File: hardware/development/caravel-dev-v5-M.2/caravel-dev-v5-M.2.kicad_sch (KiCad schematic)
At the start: 64 parts, among them J1 USB_B_Micro - 10118193-0001LF, J10 Conn_01x27_Female, J11 Conn_01x20_Female, J2 Conn_01x02_Female, J3 Conn_01x02_Male, J4 Conn_01x03_Female, J5 Conn_01x02_Male, J6 Conn_01x02_Male, J7 Conn_01x06_Female, J8 Conn_01x02_Male, J9 Conn_01x02_Male, SW1 SW_Push - SKQGADE010, T1 Logo, T2 Logo, U1 FT232H, U2 SN74LVC1G125DCKR, U3 SN74LVC1G125DCKR, U4 MCP1319MT-29LE-OT, U5 TAR5SxxU_SOT353F, U6 TAR5SxxU_SOT353F, U7 W25Q32FVSS, U8 caravel-M.2-card, X1 DSC6001_10MHZ, Y1 CSTNE12M0GH5L000R0

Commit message: ~ update caravel v5 board: ~ fix UART mode issue by enabling it by default (pull `~UART_EN` down) and in SPI mode,   the FTDI drives `~UART_EN` high. This is required since the FTDI GPIOs are not   configurable in UART mode. - remove on-board PoR U4 and use the on-chip PoR
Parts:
- removed J10: Conn_01x27_Female, Connector_PinHeader_2.54mm:PinHeader_1x27_P2.54mm_Vertical, symbol Connector:Conn_01x28_Female
- removed J11: Conn_01x20_Female, Connector_PinHeader_2.54mm:PinHeader_1x20_P2.54mm_Vertical, symbol Connector:Conn_01x28_Female
- removed J2: Conn_01x02_Female, Connector_PinHeader_2.54mm:PinHeader_1x02_P2.54mm_Vertical, symbol Connector:Conn_01x02_Female
- removed J3, J5, J6: Conn_01x02_Male, Connector_PinHeader_2.54mm:PinHeader_1x02_P2.54mm_Vertical, symbol Connector:Conn_01x02_Male
- removed J7: Conn_01x06_Female, Connector_PinHeader_2.54mm:PinHeader_1x06_P2.54mm_Vertical, symbol Connector:Conn_01x06_Female
- removed U4: MCP1319MT-29LE-OT, Caravel_Board:PoR_5_SOT23, symbol Caravel_board:MCP1319MT-29LE-OT
- removed U8: caravel-M.2-card, MicroMod-Sparkfun:M.2-CONNECTOR-E, symbol Caravel_board:caravel-M.2-card
- added C18, C21: 0.1uF, Capacitor_SMD:C_0805_2012Metric, symbol Device:C
- added C19: 1uF, Capacitor_SMD:C_0805_2012Metric, symbol Device:C
- added C20: 0.01uF, Capacitor_SMD:C_0805_2012Metric, symbol Device:C
- added C22: 10uF, Capacitor_SMD:C_0805_2012Metric, symbol Device:C
- added FB1: 600R/0.5A, Inductor_SMD:L_0805_2012Metric, symbol Device:FerriteBead
- added J10, J11: Conn_01x28_Pin, Connector_PinHeader_2.54mm:PinHeader_1x28_P2.54mm_Vertical, symbol Connector:Conn_01x28_Socket
- added J2, J3, J5, J6: Conn_01x02_Pin, Connector_PinHeader_2.54mm:PinHeader_1x02_P2.54mm_Vertical, symbol Connector:Conn_01x02_Pin
- added J7: Conn_01x06_Pin, Connector_PinHeader_2.54mm:PinHeader_1x06_P2.54mm_Vertical, symbol Connector:Conn_01x06_Pin
- added U8: M.2-CONNECTOR-E, MicroMod-Sparkfun:M.2-CONNECTOR-E, symbol MicroMod-Sparkfun:M.2-CONNECTOR-E
- C1: value 0.01uf - CC0805JRX7R9BB103 -> 0.01uF; Part # (none) -> C0805C103K5RAC7411
- C10, C13: value 1uf - CC0805KKX5R8BB105 -> 1uF; Part # (none) -> 885012207103
- C11, C14: value 0.01uf - CC0805KRX7R9BB103 -> 0.01uF; Part # (none) -> C0805C103K5RAC7411
- C12, C15: value 10uf - CC0805KKX5R8BB106 -> 10uF; Part # (none) -> CL21B106KAYQNNE
- C16: value 0.1uf - CC0805KRX7R9BB104 -> 10uF; Part # (none) -> CL21B106KAYQNNE
- C17: value 0.1uf - CC0805KRX7R9BB104 -> 0.01uF; Part # (none) -> C0805C103K5RAC7411
- C2, C3, C4, C5, C6, C7, C8, C9: value 0.1uf - CC0805KRX7R9BB104 -> 0.1uF; Part # (none) -> C0805C104K5RAC7411
- D1, D2, D3, D4: value LED - 17-215SURC/S530-A2/TR8 -> RED; Part # (none) -> LTST-C230KRKT
- J1: value USB_B_Micro - 10118193-0001LF -> USB_B_Micro; Part # (none) -> 10118193-0001LF
- J4: value Conn_01x03_Female -> Conn_01x03_Pin
- J8, J9: value Conn_01x02_Male -> Conn_01x02_Pin; symbol Connector:Conn_01x02_Male -> Connector:Conn_01x02_Pin
- R1, R10, R12, R13, R7, R8, R9: value 10k - RC0805FR-0710KL -> 10K; Part # (none) -> RC0805FR-0710KL
- R11, R14: value 82 - 0805W8F820JT5E -> 1K; Part # (none) -> RC0805FR-071KL
- R15, R16: value 10k -> 10K; Part # (none) -> RC0805FR-0710KL
- R2: value 12K 1% - 0805W8F1202T5E -> 12K 1%; Part # (none) -> RMCF0805FT12K0
- R3, R4: value 150 - 0805W8J0151T5E -> 150; Part # (none) -> RNCP0805FTD150R
- R5, R6: value 10k -> 1K; Part # (none) -> RC0805FR-071KL
- U1: Part # (none) -> FT232H
- U2, U3: Part # (none) -> SN74LVC1G125DCKR
- U5: value TAR5SxxU_SOT353F -> TAR5SxxU; Part # (none) -> TAR5S33UTE85LF
- U6: value TAR5SxxU_SOT353F -> TAR5SxxU; Part # (none) -> TAR5S18U-TE85L-F
- U7: Part # (none) -> W25Q32JVSSIQ
- X1: Part # (none) -> DSC6001JI1B
- Y1: value CSTNE12M0GH5L000R0 -> 12MHz; Part # (none) -> CSTNE12M0GH5L000R0
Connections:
- net +1V8: now also J11.22 (Pin_22), J11.23 (Pin_23), J11.24 (Pin_24), J3.1 (Pin_1), J3.2 (Pin_2), U8.14 (P14), U8.15 (P15), U8.35 (P27)
- net +5V: now also C21.2, C22.2, FB1.2; no longer J1.1 (VBUS)
- net Caravel_CSB: now also J7.1 (Pin_1), U8.11 (P11)
- net Caravel_D0: now also J7.6 (Pin_6), U8.17 (P17)
- net Caravel_D1: now also J7.2 (Pin_2), U8.19 (P19)
- net Caravel_SCK: now also J7.5 (Pin_5), U8.23 (P23)
- net GND: now also C16.2, C17.1, R5.1, R6.1, C18.2, C19.2, C20.2, C21.1, C22.1, J10.28 (Pin_28), J10.6 (Pin_6), J11.1 (Pin_1), J11.17 (Pin_17), J11.18 (Pin_18), J11.28 (Pin_28), J6.2 (Pin_2), U8.12 (P12), U8.18 (P18), U8.37 (P29), U8.A1 (GND), U8.A2 (GND); no longer C16.1, C17.2
- net USB_CS1: now also J11.12 (Pin_12), U8.55 (P47)
- net USB_SCK_TXD: now also J11.11 (Pin_11), U8.57 (P49)
- net USB_SI: now also J11.14 (Pin_14), U8.51 (P43)
- net USB_SO_RXD: now also J11.13 (Pin_13), U8.53 (P45)
- net gpio: now also J11.20 (Pin_20), U8.21 (P21)
- net mprj_io[0]: now also J11.15 (Pin_15), U8.49 (P41)
- net mprj_io[10]: now also J11.5 (Pin_5), U8.69 (P61)
- net mprj_io[11]: now also J11.4 (Pin_4), U8.71 (P63)
- net mprj_io[12]: now also J11.3 (Pin_3), U8.73 (P65)
- net mprj_io[13]: now also J11.2 (Pin_2), U8.75 (P67)
- net mprj_io[14]: now also J10.27 (Pin_27), U8.74 (P66)
- net mprj_io[15]: now also J10.26 (Pin_26), U8.72 (P64)
- net mprj_io[16]: now also J10.25 (Pin_25), U8.70 (P62)
- net mprj_io[17]: now also J10.24 (Pin_24), U8.68 (P60)
- net mprj_io[18]: now also J10.23 (Pin_23), U8.66 (P58)
- net mprj_io[19]: now also J10.22 (Pin_22), U8.64 (P56)
- net mprj_io[20]: now also J10.21 (Pin_21), U8.62 (P54)
- net mprj_io[21]: now also J10.20 (Pin_20), U8.60 (P52)
- net mprj_io[22]: now also J10.19 (Pin_19), U8.58 (P50)
- net mprj_io[23]: now also J10.18 (Pin_18), U8.56 (P48)
- net mprj_io[24]: now also J10.17 (Pin_17), U8.54 (P46)
- net mprj_io[25]: now also J10.16 (Pin_16), U8.52 (P44)
- net mprj_io[26]: now also J10.15 (Pin_15), U8.50 (P42)
- net mprj_io[27]: now also J10.14 (Pin_14), U8.48 (P40)
- net mprj_io[28]: now also J10.13 (Pin_13), U8.46 (P38)
- net mprj_io[29]: now also J10.12 (Pin_12), U8.44 (P36)
- net mprj_io[30]: now also J10.11 (Pin_11), U8.42 (P34)
- net mprj_io[31]: now also J10.10 (Pin_10), U8.40 (P32)
- net mprj_io[32]: now also J10.9 (Pin_9), U8.38 (P30)
- net mprj_io[33]: now also J10.8 (Pin_8), U8.36 (P28)
- net mprj_io[34]: now also J10.4 (Pin_4), U8.34 (P26)
- net mprj_io[35]: now also J10.3 (Pin_3), U8.32 (P24)
- net mprj_io[36]: now also J10.2 (Pin_2), U8.22 (P22)
- net mprj_io[37]: now also J10.1 (Pin_1), U8.20 (P20)
- net mprj_io[5]_ser_rx: now also J11.10 (Pin_10), U8.59 (P51)
- net mprj_io[6]_ser_tx: now also J11.9 (Pin_9), U8.61 (P53)
- net mprj_io[7]: now also J11.8 (Pin_8), U8.63 (P55)
- net mprj_io[8]: now also J11.7 (Pin_7), U8.65 (P57)
- net mprj_io[9]: now also J11.6 (Pin_6), U8.67 (P59)
- net vccd2: now also J11.21 (Pin_21), U8.1 (P1)
- net vdda1: now also J11.16 (Pin_16), U8.33 (P25)
- net vdda2: now also J11.25 (Pin_25), U8.13 (P13)
- net xclk: now also J11.19 (Pin_19), U8.9 (P9)
- net ~{MEM_HOLD}: now also J7.4 (Pin_4)
- net ~{MEM_WP}: now also J7.3 (Pin_3)
- net VCCA: now reaches C3.2, U1.37 (VCCA)
- net OSC_EN: now reaches X1.1 (EN)
- net OSC_EN: now also J6.1 (Pin_1)
- net Noise_3V3: now reaches C11.1, U5.3 (Noise)
- net ~{FTDI_RST}: now reaches C1.2, R1.1, U1.34 (~{RESET})
- net VCCCORE: now reaches C2.2, U1.38 (VCCCORE)
- net ACBUS2: now reaches D1.1 (K)
- net ACBUS2: now also U1.26 (ACBUS2); no longer U1.27 (ACBUS3)
- net Noise_1V8: now reaches C14.1, U6.3 (Noise)
- net ADBUS4: now reaches U1.17 (ADBUS4)
- net ADBUS5: now reaches U1.18 (ADBUS5)
- net ADBUS6: now reaches U1.19 (ADBUS6)
- net ADBUS7: now reaches U1.20 (ADBUS7)
- net ACBUS3: now reaches D2.1 (K)
- net ACBUS3: now also U1.27 (ACBUS3); no longer U1.26 (ACBUS2)
- net ACBUS4: now reaches U1.28 (ACBUS4)
- net ACBUS5: now reaches U1.29 (ACBUS5)
- net ACBUS6: now reaches U1.30 (ACBUS6)
- net ACBUS7: now reaches U1.31 (ACBUS7)
- net +3.3V renamed +3V3
- net +3V3: now also C16.1, C17.2, C18.1, C19.1, J10.7 (Pin_7), J11.26 (Pin_26), J11.27 (Pin_27), J2.1 (Pin_1), J5.1 (Pin_1), J5.2 (Pin_2), U8.16 (P16), U8.3 (P3), U8.5 (P5); no longer C16.2, C17.1, R5.1, R6.1
- net UART_EN renamed ACBUS0
- net ACBUS0: now also J2.2 (Pin_2)
- net ~{MR} renamed ACBUS1
- net ACBUS1: now also J10.5 (Pin_5), U8.7 (P7)
- new net VBUS: C20.1, FB1.1, J1.1 (VBUS)
- no-connect marks 26 -> 17
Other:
- note added: "*ACBUS7 pulled-down"
- note added: "*ACBUS8-9 are not configurable as GPIOs in MPSSE mode"
- note added: "*Place close to the USB connector"
- note added: "*enabled by default and should be disabled in SPI mode"
- note added: "*required since the FTDI UART ports are shared with the SPI"
- note added: "Buffers to enable FTDI UART interface with Caravel"
- note added: "Caravel M.2 Card"
- note added: "Caravel Power Pin Headers"
- note added: "FTDI SPI interface with HKSPI"
- note added: "GPIO Connectors"
- note added: "Interfaces"
- note added: "M.2 Connector + Peripherals"
- note added: "Pin Headers"
- note added: "Power"
- note added: "Reset"
- note added: "Reset Switch"
- note added: "USB to Serial"
- note added: "VBUS Filter to 5V"
- note added: "Voltage Regulators"
- note added: "internally with 75k by default"
- note removed: "Buffers to enable FTDI UART interface"
- note removed: "FTDI interface with HKSPI"
- note removed: "IO Connectors"
- note removed: "Power Pin Headers"
- note removed: "Power on Reset"
- note removed: "Voltage Regulator"
- company: (none) -> Efabless
- title: (none) -> Caravel 3.3V Development Board
- moved on the sheet: C10, C11, C12, C13, C14, C15, J8, J9, R15, R16, U5, U6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

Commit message: ~ update caravel REV5B board files
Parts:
- added TP3, TP4, TP5, TP6: TestPoint, TestPoint:TestPoint_Loop_D1.80mm_Drill1.0mm_Beaded, symbol Connector:TestPoint
- U2, U3: footprint SOT65P210X110-5N -> strive_foot_prints:SOT65P210X110-5N
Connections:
- net +3V3: now also J10.3 (Pin_3); no longer J10.7 (Pin_7)
- net ACBUS1: now also J10.1 (Pin_1); no longer J10.5 (Pin_5)
- net ADBUS4: now also TP3.1
- net ADBUS5: now also TP4.1
- net ADBUS6: now also TP5.1
- net ADBUS7: now also TP6.1
- net GND: now also J10.2 (Pin_2); no longer J10.6 (Pin_6)
- net mprj_io[34]: now also J10.7 (Pin_7); no longer J10.4 (Pin_4)
- net mprj_io[35]: now also J10.6 (Pin_6); no longer J10.3 (Pin_3)
- net mprj_io[36]: now also J10.5 (Pin_5); no longer J10.2 (Pin_2)
- net mprj_io[37]: now also J10.4 (Pin_4); no longer J10.1 (Pin_1)

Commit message: ~ update caravel REV5B
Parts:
- removed TP3, TP4, TP5, TP6: TestPoint, TestPoint:TestPoint_Loop_D1.80mm_Drill1.0mm_Beaded, symbol Connector:TestPoint
- added J12: Conn_01x04_Pin, Connector_PinHeader_2.54mm:PinHeader_1x04_P2.54mm_Vertical, symbol Connector:Conn_01x04_Pin
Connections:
- net ADBUS4: now also J12.1 (Pin_1)
- net ADBUS5: now also J12.2 (Pin_2)
- net ADBUS6: now also J12.3 (Pin_3)
- net ADBUS7: now also J12.4 (Pin_4)
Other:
- note added: "*exposed GPIOs"
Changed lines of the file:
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@@
   (junction (at 260.731 196.596) (diameter 0) (color 0 0 0 0)
   )
+  (junction (at 223.774 244.856) (diameter 0) (color 0 0 0 0)
+  )
   (junction (at 279.781 106.426) (diameter 0) (color 0 0 0 0)
   )
@@
   (junction (at 356.616 208.28) (diameter 0) (color 0 0 0 0)
   )
-  (junction (at 151.13 75.438) (diameter 0) (color 0 0 0 0)
-  )
   (junction (at 272.161 92.456) (diameter 0) (color 0 0 0 0)
   )
+  (junction (at 226.314 244.856) (diameter 0) (color 0 0 0 0)
+  )
   (junction (at 303.784 149.606) (diameter 0) (color 0 0 0 0)
   )
@@
   (junction (at 253.111 196.596) (diameter 0) (color 0 0 0 0)
   )
-  (junction (at 285.115 244.348) (diameter 0) (color 0 0 0 0)
-  )
-  (junction (at 129.54 77.978) (diameter 0) (color 0 0 0 0)
-  )
   (junction (at 162.052 247.142) (diameter 0) (color 0 0 0 0)
   )
@@
   (junction (at 373.634 190.5) (diameter 0) (color 0 0 0 0)
   )
-  (junction (at 287.655 244.348) (diameter 0) (color 0 0 0 0)
-  )
   (junction (at 382.016 164.465) (diameter 0) (color 0 0 0 0)
   )
@@
   (junction (at 330.708 164.338) (diameter 0) (color 0 0 0 0)
   )
-  (junction (at 151.13 77.978) (diameter 0) (color 0 0 0 0)
+  (junction (at 129.54 77.978) (diameter 0) (color 0 0 0 0)
   )
-  (junction (at 223.774 244.856) (diameter 0) (color 0 0 0 0)
+  (junction (at 285.115 244.348) (diameter 0) (color 0 0 0 0)
   )
-  (junction (at 226.314 244.856) (diameter 0) (color 0 0 0 0)
+  (junction (at 151.13 77.978) (diameter 0) (color 0 0 0 0)
+  )
+  (junction (at 287.655 244.348) (diameter 0) (color 0 0 0 0)
   )
   (junction (at 263.271 196.596) (diameter 0) (color 0 0 0 0)
@@
   (junction (at 248.031 110.236) (diameter 0) (color 0 0 0 0)
   )
+  (junction (at 151.13 75.438) (diameter 0) (color 0 0 0 0)
+  )
   (junction (at 239.395 246.888) (diameter 0) (color 0 0 0 0)
   )
@@
     (stroke (width 0) (type default))
   )
+  (wire (pts (xy 285.115 244.348) (xy 287.655 244.348))
+    (stroke (width 0) (type default))
+  )
   (wire (pts (xy 71.12 36.068) (xy 54.61 36.068))
     (stroke (width 0) (type default))
@@
     (stroke (width 0) (type default))
   )
+  (wire (pts (xy 129.54 75.438) (xy 129.54 77.978))
+    (stroke (width 0) (type default))
+  )
   (wire (pts (xy 282.575 244.348) (xy 285.115 244.348))
     (stroke (width 0) (type default))
@@
     (stroke (width 0) (type default))
   )
+  (wire (pts (xy 223.774 244.856) (xy 226.314 244.856))
+    (stroke (width 0) (type default))
+  )
   (wire (pts (xy 92.456 161.29) (xy 83.82 161.29))
     (stroke (width 0) (type default))
@@
     (stroke (width 0) (type default))
   )
+  (wire (pts (xy 151.13 75.438) (xy 151.13 77.978))
+    (stroke (width 0) (type default))
+  )
   (wire (pts (xy 273.431 129.286) (xy 282.829 129.286))
     (stroke (width 0) (type default))
@@
     (stroke (width 0) (type default))
   )
-  (wire (pts (xy 129.54 75.438) (xy 129.54 77.978))
-    (stroke (width 0) (type default))
-  )
   (wire (pts (xy 58.293 132.715) (xy 58.293 134.239))
     (stroke (width 0) (type default))
@@
     (stroke (width 0) (type default))
   )
-  (wire (pts (xy 151.13 75.438) (xy 151.13 77.978))
-    (stroke (width 0) (type default))
-  )
   (polyline (pts (xy 187.833 112.903) (xy 15.113 112.903))
     (stroke (width 0) (type dash))
@@
     (stroke (width 0) (type default))
   )
-  (wire (pts (xy 285.115 244.348) (xy 287.655 244.348))
-    (stroke (width 0) (type default))
-  )
   (wire (pts (xy 135.89 77.978) (xy 129.54 77.978))
     (stroke (width 0) (type default))
@@
     (stroke (width 0) (type default))
   )
-  (wire (pts (xy 223.774 244.856) (xy 226.314 244.856))
-    (stroke (width 0) (type default))
-  )
   (wire (pts (xy 178.054 257.556) (xy 200.914 257.556))
     (stroke (width 0) (type default))
@@
     (effects (font (size 1.5 1.5)) (justify left bottom))
   )
+  (text "*exposed GPIOs" (at 287.909 136.144 0)
+    (effects (font (size 1.25 1.25)) (justify left bottom))
+  )
   (text "Power" (at 116.459 225.171 0)
     (effects (font (size 3.5 3.5) (thickness 0.7) bold italic) (justify left bottom))
@@
     )
   )
-  (symbol (lib_id "Connector:TestPoint") (at 281.432 139.446 270) (unit 1)
-    (in_bom yes) (on_board yes) (dnp no)
-    (property "Reference" "TP6" (at 286.004 139.573 90)
-      (effects (font (size 1.27 1.27)) (justify left))
-    )
-    (property "Value" "TestPoint" (at 286.893 140.716 90)
-      (effects (font (size 1.27 1.27)) (justify left) hide)
-    )
-    (property "Footprint" "TestPoint:TestPoint_Loop_D1.80mm_Drill1.0mm_Beaded" (at 281.432 144.526 0)
-      (effects (font (size 1.27 1.27)) hide)
-    )
-    (property "Datasheet" "~" (at 281.432 144.526 0)
-      (effects (font (size 1.27 1.27)) hide)
-    )
-    (pin "1")
-    (instances
-      (project "caravel-dev-v5-M.2"
-        (path "/6d7a4d05-3bd6-4623-a293-816712af04ea"
-          (reference "TP6") (unit 1)
-        )
-      )
-    )
-  )
   (symbol (lib_id "Connector:USB_B_Micro") (at 212.979 100.584 0) (unit 1)
     (in_bom yes) (on_board yes) (dnp no)
@@
     )
   )
+  (symbol (lib_id "Connector:Conn_01x04_Pin") (at 286.512 134.366 0) (mirror y) (unit 1)
+    (in_bom yes) (on_board yes) (dnp no)
+    (property "Reference" "J12" (at 289.433 132.08 0)
+      (effects (font (size 1.27 1.27)))
+    )
+    (property "Value" "Conn_01x04_Pin" (at 291.973 135.636 90)
+      (effects (font (size 1.27 1.27)) hide)
+    )
+    (property "Footprint" "Connector_PinHeader_2.54mm:PinHeader_1x04_P2.54mm_Vertical" (at 286.512 134.366 0)
+      (effects (font (size 1.27 1.27)) hide)
+    )
+    (property "Datasheet" "~" (at 286.512 134.366 0)
+      (effects (font (size 1.27 1.27)) hide)
+    )
+    (pin "1")
+    (pin "3")
+    (pin "2")
+    (pin "4")
+    (instances
+      (project "caravel-dev-v5-M.2"
+        (path "/6d7a4d05-3bd6-4623-a293-816712af04ea"
+          (reference "J12") (unit 1)
+        )
+      )
+    )
+  )
   (symbol (lib_id "power:GND") (at 149.86 259.334 0) (unit 1)
     (in_bom yes) (on_board yes) (dnp no)
@@
     )
   )
-  (symbol (lib_id "Connector:TestPoint") (at 281.432 134.366 270) (unit 1)
-    (in_bom yes) (on_board yes) (dnp no)
-    (property "Reference" "TP4" (at 286.004 134.493 90)
-      (effects (font (size 1.27 1.27)) (justify left))
-    )
-    (property "Value" "TestPoint" (at 286.893 135.636 90)
-      (effects (font (size 1.27 1.27)) (justify left) hide)
-    )
-    (property "Footprint" "TestPoint:TestPoint_Loop_D1.80mm_Drill1.0mm_Beaded" (at 281.432 139.446 0)
-      (effects (font (size 1.27 1.27)) hide)
-    )
-    (property "Datasheet" "~" (at 281.432 139.446 0)
-      (effects (font (size 1.27 1.27)) hide)
-    )
-    (pin "1")
-    (instances
-      (project "caravel-dev-v5-M.2"
-        (path "/6d7a4d05-3bd6-4623-a293-816712af04ea"
-          (reference "TP4") (unit 1)
-        )
-      )
-    )
-  )
   (symbol (lib_id "Device:R") (at 299.212 157.607 90) (unit 1)
     (in_bom yes) (on_board yes) (dnp no)
@@
     )
   )
-  (symbol (lib_id "Connector:TestPoint") (at 281.432 131.826 270) (unit 1)
-    (in_bom yes) (on_board yes) (dnp no)
-    (property "Reference" "TP3" (at 286.004 131.826 90)
-      (effects (font (size 1.27 1.27)) (justify left))
-    )
-    (property "Value" "TestPoint" (at 286.893 133.096 90)
-      (effects (font (size 1.27 1.27)) (justify left) hide)
-    )
-    (property "Footprint" "TestPoint:TestPoint_Loop_D1.80mm_Drill1.0mm_Beaded" (at 281.432 136.906 0)
-      (effects (font (size 1.27 1.27)) hide)
-    )
-    (property "Datasheet" "~" (at 281.432 136.906 0)
-      (effects (font (size 1.27 1.27)) hide)
-    )
-    (pin "1")
-    (instances
-      (project "caravel-dev-v5-M.2"
-        (path "/6d7a4d05-3bd6-4623-a293-816712af04ea"
-          (reference "TP3") (unit 1)
-        )
-      )
-    )
-  )
   (symbol (lib_id "Device:C") (at 208.153 125.222 90) (unit 1)
     (in_bom yes) (on_board yes) (dnp no)
@@
         )
       )
-    )
-  )
-  (symbol (lib_id "Connector:TestPoint") (at 281.432 136.906 270) (unit 1)
-    (in_bom yes) (on_board yes) (dnp no)
-    (property "Reference" "TP5" (at 286.004 137.033 90)
-      (effects (font (size 1.27 1.27)) (justify left))
-    )
-    (property "Value" "TestPoint" (at 286.893 138.176 90)
-      (effects (font (size 1.27 1.27)) (justify left) hide)
-    )
-    (property "Footprint" "TestPoint:TestPoint_Loop_D1.80mm_Drill1.0mm_Beaded" (at 281.432 141.986 0)
-      (effects (font (size 1.27 1.27)) hide)
-    )
-    (property "Datasheet" "~" (at 281.432 141.986 0)
-      (effects (font (size 1.27 1.27)) hide)
-    )
-    (pin "1")
-    (instances
-      (project "caravel-dev-v5-M.2"
-        (path "/6d7a4d05-3bd6-4623-a293-816712af04ea"
-          (reference "TP5") (unit 1)
-        )
-      )

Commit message: ~ update caravel REV 5B with larger logos
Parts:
- T1: footprint Caravel_Board:logo -> Caravel_Board:logo_large
- T2: footprint Caravel_Board:ef_logo -> Caravel_Board:ef_logo_large
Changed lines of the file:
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@@
       (effects (font (size 1.27 1.27)) (justify left))
     )
-    (property "Footprint" "Caravel_Board:logo" (at 144.145 32.258 0)
+    (property "Footprint" "Caravel_Board:logo_large" (at 144.145 32.258 0)
       (effects (font (size 1.27 1.27)) hide)
     )
@@
       (effects (font (size 1.27 1.27)) (justify left))
     )
-    (property "Footprint" "Caravel_Board:ef_logo" (at 156.845 32.258 0)
-      (effects (font (size 1.27 1.27)) hide)
-    )
+    (property "Footprint" "Caravel_Board:ef_logo_large" (at 156.845 32.258 0)
+      (effects (font (size 1.27 1.27)) hide)
+    )

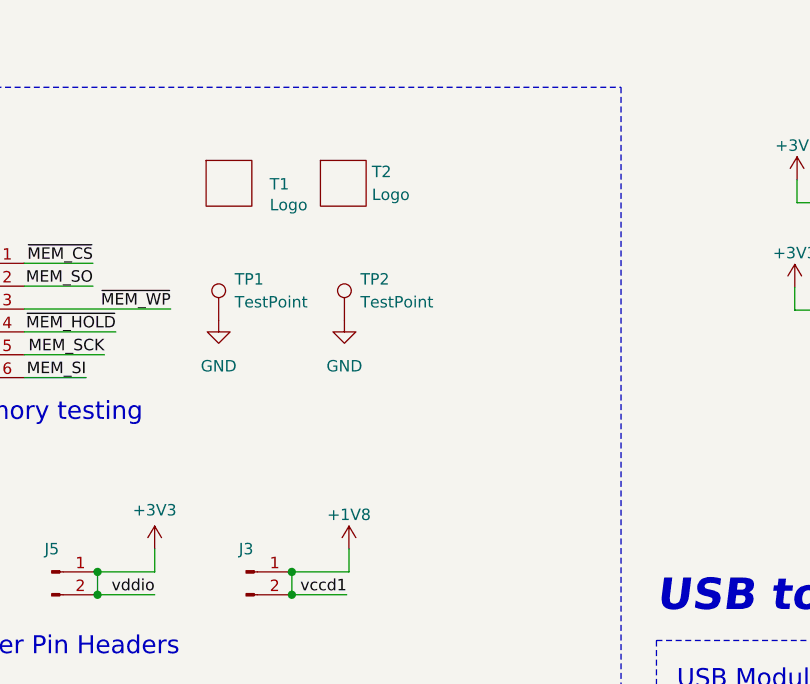
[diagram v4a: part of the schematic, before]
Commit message: ~ update caravel REV 5B logos
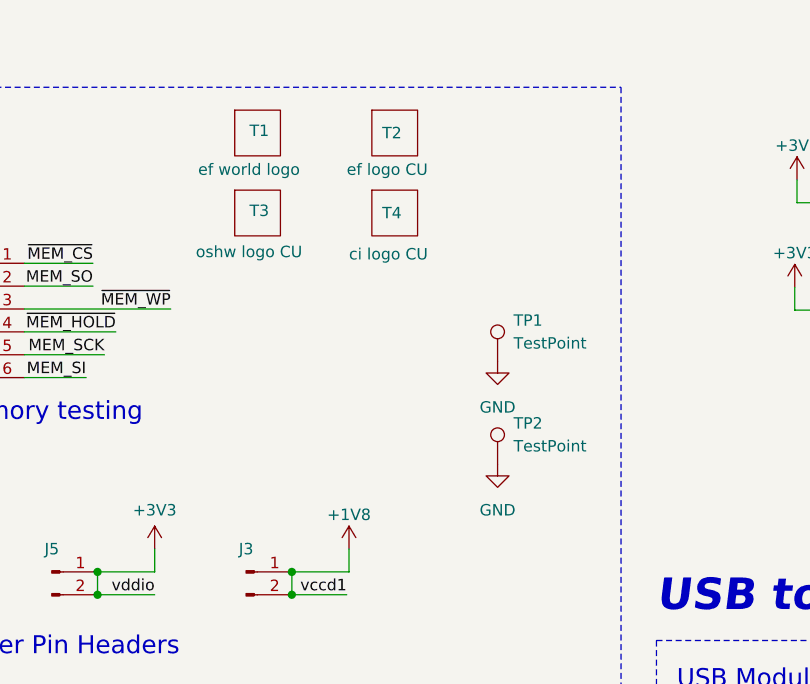
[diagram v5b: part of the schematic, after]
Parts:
- added T3: oshw logo CU, Caravel_Board:oshw-logo, symbol Caravel_board:Logo
- added T4: ci logo CU, Caravel_Board:chipIgnite_logo, symbol Caravel_board:Logo
- T1: value Logo -> ef world logo
- T2: value Logo -> ef logo CU; footprint Caravel_Board:ef_logo_large -> Caravel_Board:ef_logo-cu
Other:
- moved on the sheet: T1, T2, TP1, TP2
